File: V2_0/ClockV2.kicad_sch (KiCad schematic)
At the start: 30 parts, among them J101 Conn_Coaxial, J103 Conn_02x04_Odd_Even, J104 Conn_02x04_Odd_Even, J105 DIN41612_02x16_AC_EvenPins, SW101 SW_Push, U102 LM1117DT-3.3, U103 CA56-12CGKWA, U104 ADP7142ARDZ-2.5

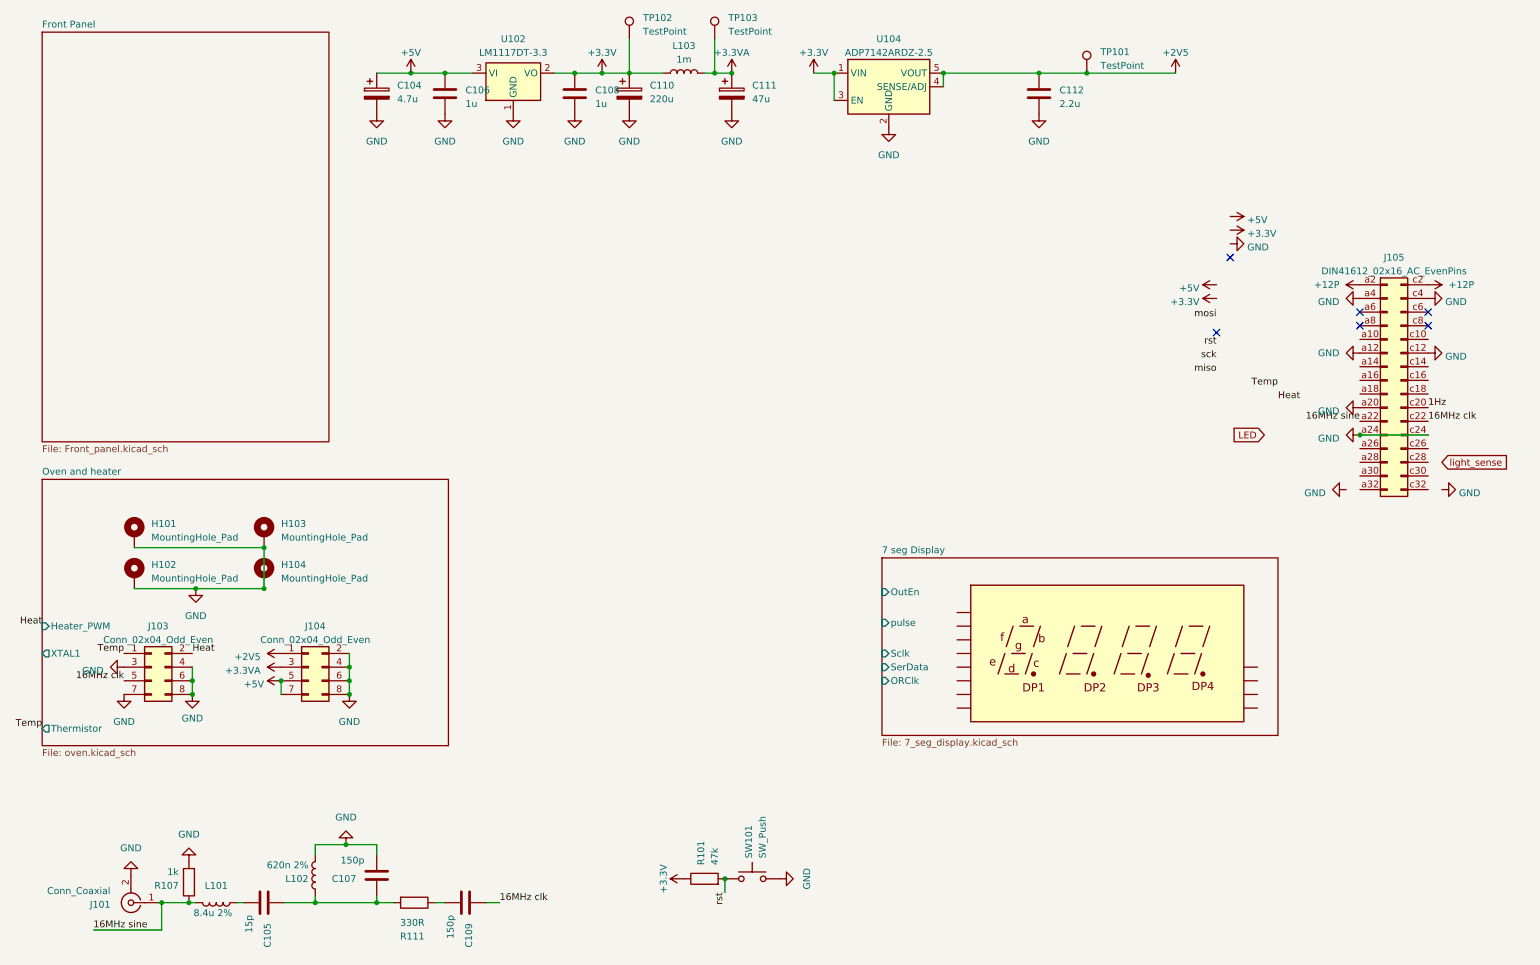
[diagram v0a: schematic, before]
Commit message: New Kicad Project for V2.1
moved the V2 to a new folder and made V2.1 folder for STM32 version
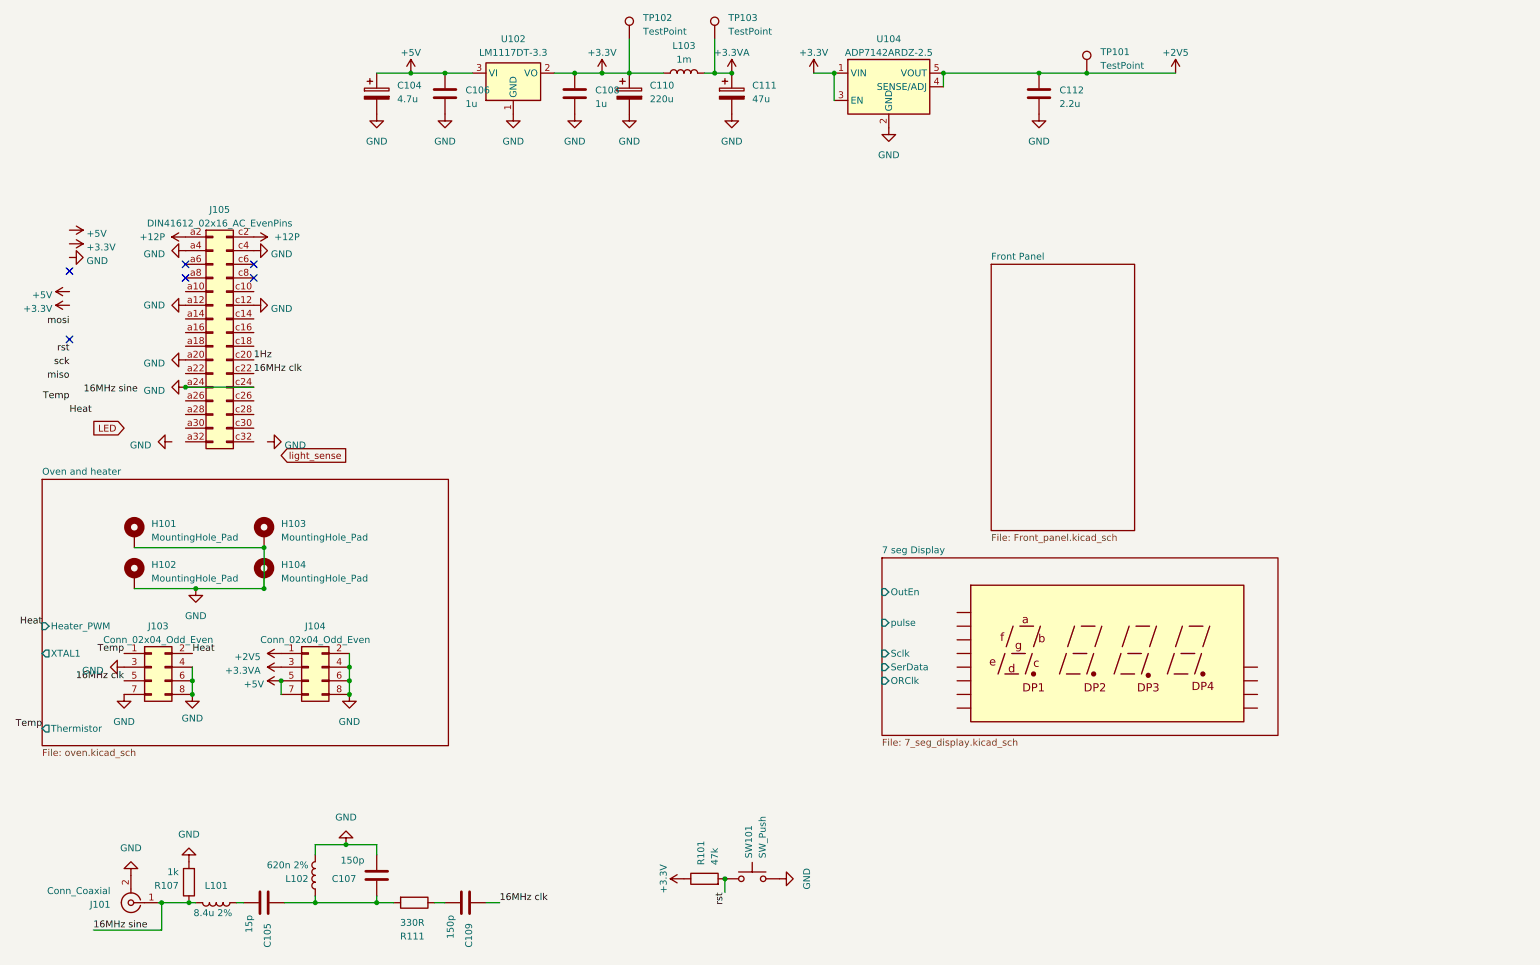
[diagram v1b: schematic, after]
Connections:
- net 16MHz sine: no longer J105.a22 (Pin_a22)
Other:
- moved on the sheet: J105
